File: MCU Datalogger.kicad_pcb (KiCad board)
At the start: 2 copper layers, 51.4 x 34.3 mm, 32 parts, among them J1 Conn_01x04_Male, J2 Conn_01x09_Male, J3 Conn_01x04_Male, J4 Conn_02x03_Odd_Even, U1 24LC1025, U2 DS1337S+, U3 24LC1025, U4 ATMEGA328P-AU, Y1 32.768 KHz, Y2 16 MHz

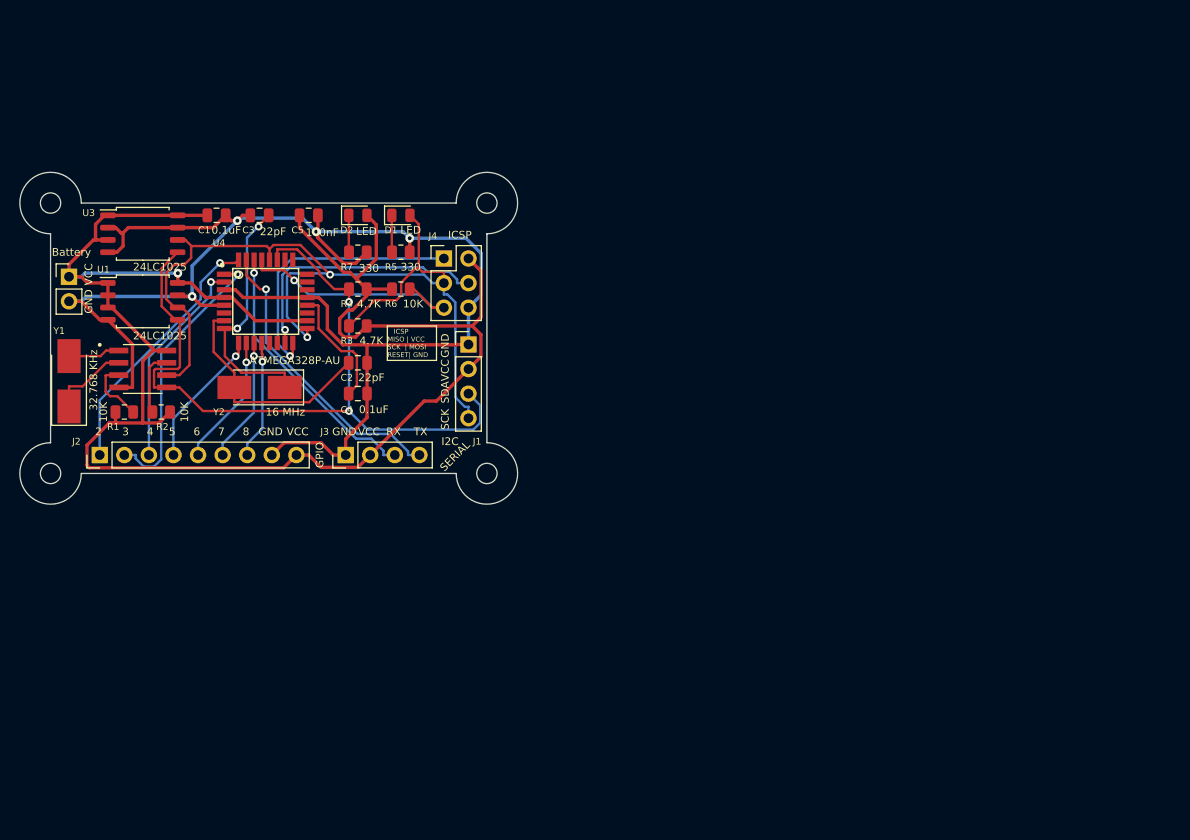
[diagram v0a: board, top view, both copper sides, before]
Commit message: :memo: first change of mcu datalogger
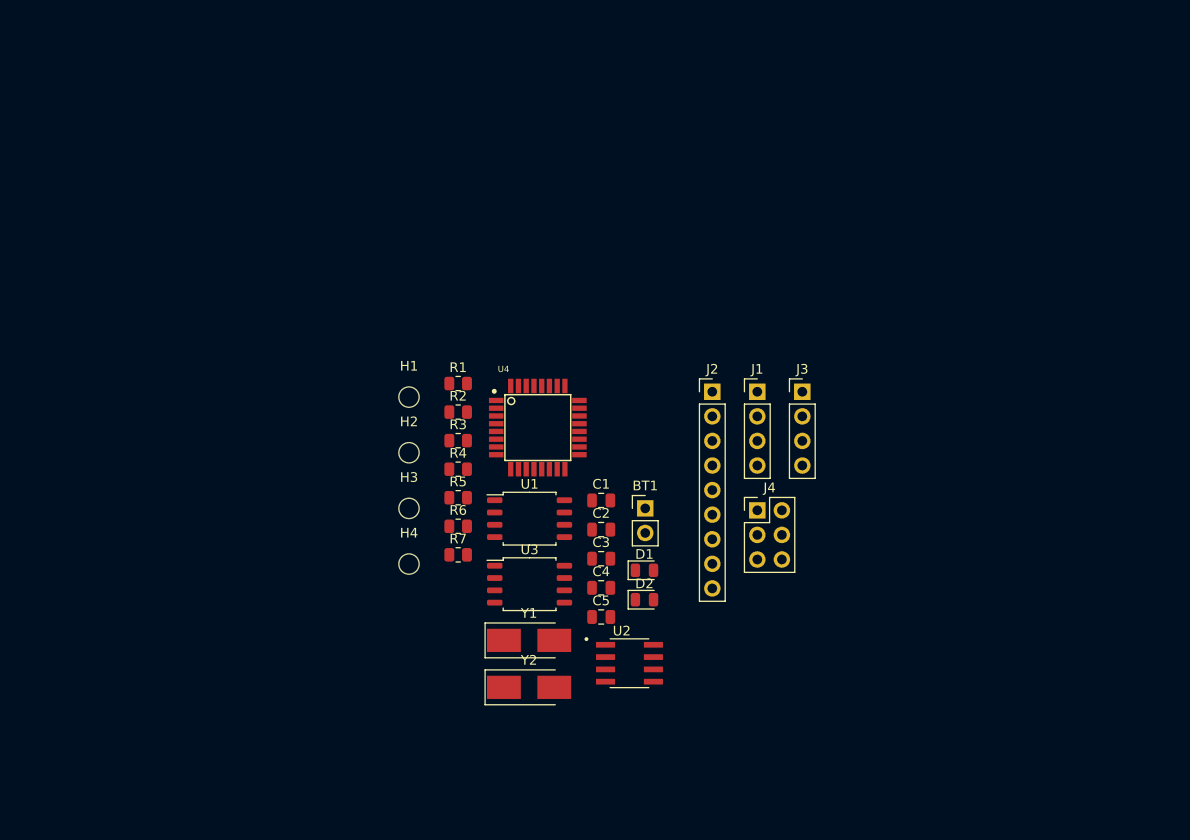
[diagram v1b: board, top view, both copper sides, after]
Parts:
- removed G***: LOGO, Footprints:TE_Logo_10mm_negative_silkscreen
- removed G2: LOGO, DesktopLibrary:TE_Logo_11.6x4
- removed REF1: KiCad-Logo2_5mm_SilkScreen, Symbol:KiCad-Logo2_5mm_SilkScreen
- moved BT1 64.2 mm to (153.5, 106.5)
- moved J2 63.6 mm to (160.4, 94.4), turned to 0 degrees
- moved U2 58.8 mm to (151.9, 122.5)
- moved Y1 54.6 mm to (141.5, 120.1), turned to 0 degrees
- moved U3 53.9 mm to (141.6, 114.3)
- moved C5 51.3 mm to (149.0, 117.7)
- moved C3 50.1 mm to (149.0, 111.7)
- moved D2 49.5 mm to (153.4, 115.9)
- moved C1 49.5 mm to (149.0, 105.7)
- moved J3 47.6 mm to (169.8, 94.4), turned to 0 degrees
- moved U1 45.8 mm to (141.6, 107.5)
- moved D1 44.5 mm to (153.4, 112.9)
- moved H1 42.1 mm to (129.1, 95.0)
- moved Y2 41.7 mm to (141.5, 125.0), turned to 0 degrees
- moved J4 41.5 mm to (165.1, 106.7)
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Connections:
- U4 pad 13: (no net) -> unconnected-(U4-PB1-Pad13)
- U4 pad 14: (no net) -> unconnected-(U4-PB2-Pad14)
- U4 pad 19: (no net) -> unconnected-(U4-ADC6-Pad19)
- U4 pad 22: (no net) -> unconnected-(U4-ADC7-Pad22)
- U4 pad 23: (no net) -> unconnected-(U4-PC0-Pad23)
- U4 pad 24: (no net) -> unconnected-(U4-PC1-Pad24)
- U4 pad 25: (no net) -> unconnected-(U4-PC2-Pad25)
- U4 pad 26: (no net) -> unconnected-(U4-PC3-Pad26)
- U4 pad 6: (no net) -> unconnected-(U4-VCC-Pad6)
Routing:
- net /Vcc: track 182.9 -> 0.00 mm, vias 1 -> 0
- net GND: track 158.8 -> 0.00 mm, vias 4 -> 0
- net /SCK: track 97.4 -> 0.00 mm, vias 2 -> 0
- net /SDA: track 80.3 -> 0.00 mm, vias 2 -> 0
- net /TX: track 30.6 -> 0.00 mm, vias 1 -> 0
- net /D3: track 28.6 -> 0.00 mm, vias 1 -> 0
- net /MISO: track 28.4 -> 0.00 mm, vias 1 -> 0
- net /RX: track 27.8 -> 0.00 mm, vias 1 -> 0
- net /MOSI: track 27.6 -> 0.00 mm, vias 1 -> 0
- net /D2: track 27.0 -> 0.00 mm, vias 1 -> 0
- net /RESET: track 25.8 -> 0.00 mm, vias 1 -> 0
- net Net-(U4-PB7): track 25.7 -> 0.00 mm, vias 2 -> 0
- net Net-(U4-PB6): track 23.9 -> 0.00 mm
- net /D4: track 21.9 -> 0.00 mm, vias 1 -> 0
- net /D5: track 14.4 -> 0.00 mm, vias 1 -> 0
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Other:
- board outline removed
- board text removed: "- 2Mbit EEPROM - RTC - I2C, SPI, GPIOs"
- board text removed: "0.2000 mm / 0.0000 mm"
- board text removed: "0.3000 mm"
- board text removed: "1.6000 mm"
- board text removed: "2"
- board text removed: "3"
- board text removed: "4"
- board text removed: "5"
- board text removed: "51.7350 mm x 34.5900 mm"
- board text removed: "6"
- board text removed: "7"
- board text removed: "8"
- board text removed: "BOARD CHARACTERISTICS"
- board text removed: "Board Thickness:"
- board text removed: "Board overall dimensions:"
- board text removed: "Castellated pads:"
- board text removed: "Copper Finish:"
- board text removed: "Copper Layer Count:"
- board text removed: "Data logger with the ATMega328P."
- board text removed: "GND"
- board text removed: "GPIO"
- board text removed: "I2C"
- board text removed: "ICSP"
- board text removed: "ICSP MISO | VCC SCK | MOSI RESET| GND"
- board text removed: "Impedance Control:"
- board text removed: "Min hole diameter:"
- board text removed: "Min track/spacing:"
- board text removed: "No"
- board text removed: "None"
- board text removed: "Plated Board Edge:"
- board text removed: "RX"
- board text removed: "SCK"
- board text removed: "SDA"
- board text removed: "SERIAL"
- board text removed: "TX"
- board text removed: "VCC"

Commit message: :memo: after autorouting
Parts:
- moved U1 42.6 mm to (119.4, 71.1)
- moved U3 42.6 mm to (119.4, 77.9)
- moved Y1 39.3 mm to (104.1, 132.1)
- moved Y2 39.3 mm to (104.1, 136.9)
- moved C5 35.8 mm to (182.4, 130.5)
- moved U2 35.8 mm to (185.4, 135.3)
- moved J1 31.7 mm to (192.6, 78.7)
- moved J2 31.7 mm to (188.0, 78.7)
- moved J4 31.7 mm to (192.6, 91.0)
- moved J3 31.7 mm to (197.3, 78.7)
- moved U4 27.5 mm to (154.9, 73.7)
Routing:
- net /SCK: track 0.00 -> 284.0 mm
- net GND: track 0.00 -> 258.8 mm, vias 0 -> 2
- net /Vcc: track 0.00 -> 252.7 mm, vias 0 -> 1
- net /SDA: track 0.00 -> 193.3 mm, vias 0 -> 2
- net /RESET: track 0.00 -> 136.3 mm, vias 0 -> 1
- net Net-(U4-PB7): track 0.00 -> 96.6 mm, vias 0 -> 3
- net Net-(U4-PB6): track 0.00 -> 90.2 mm, vias 0 -> 3
- net /D4: track 0.00 -> 83.6 mm
- net Net-(U2-X2): track 0.00 -> 83.3 mm
- net /D3: track 0.00 -> 80.0 mm
- net Net-(U2-X1): track 0.00 -> 76.7 mm
- net Net-(U2-SQW/~INT): track 0.00 -> 74.8 mm, vias 0 -> 2
- net Net-(U2-~INTA): track 0.00 -> 73.5 mm, vias 0 -> 2
- net /TX: track 0.00 -> 61.7 mm
- net /RX: track 0.00 -> 57.3 mm
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
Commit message: :memo: working temp version of schematic
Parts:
- moved J1 24.9 mm to (175.0, 61.2)
- moved J2 24.9 mm to (170.3, 61.2)
- moved J4 24.9 mm to (175.0, 73.5)
- moved J3 24.9 mm to (179.7, 61.2)
- moved C5 22.1 mm to (170.6, 111.9)
- moved U2 22.1 mm to (173.5, 116.6)
- moved Y1 21.7 mm to (118.6, 116.0)
- moved Y2 21.7 mm to (118.6, 120.8)
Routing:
- net /D4: track 83.6 -> 21.9 mm, vias 0 -> 1
- net /RESET: track 136.3 -> 77.2 mm, vias 1 -> 3
- net /D3: track 80.0 -> 23.7 mm
- net (no net): track 45.1 -> 0.00 mm, vias 3 -> 0
- net /SCK: track 284.0 -> 244.1 mm, vias 0 -> 1
- net /SDA: track 193.3 -> 153.7 mm
- net GND: track 258.8 -> 221.9 mm
- net /Vcc: track 252.7 -> 219.8 mm, vias 1 -> 3
- net /RX: track 57.3 -> 28.3 mm
- net /D6: track 56.0 -> 29.8 mm
- net Net-(U2-X2): track 83.3 -> 57.4 mm
- net Net-(U2-X1): track 76.7 -> 51.5 mm
- net /D8: track 40.9 -> 18.3 mm, vias 1 -> 0
- net Net-(U2-SQW/~INT): track 74.8 -> 52.6 mm, vias 2 -> 0
- net /TX: track 61.7 -> 41.8 mm, vias 0 -> 1
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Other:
- board outline added: 104.7 x 71 mm
